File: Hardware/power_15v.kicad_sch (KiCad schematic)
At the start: 13 parts, among them U3 TPS563200, U4 AMS1117-3.3

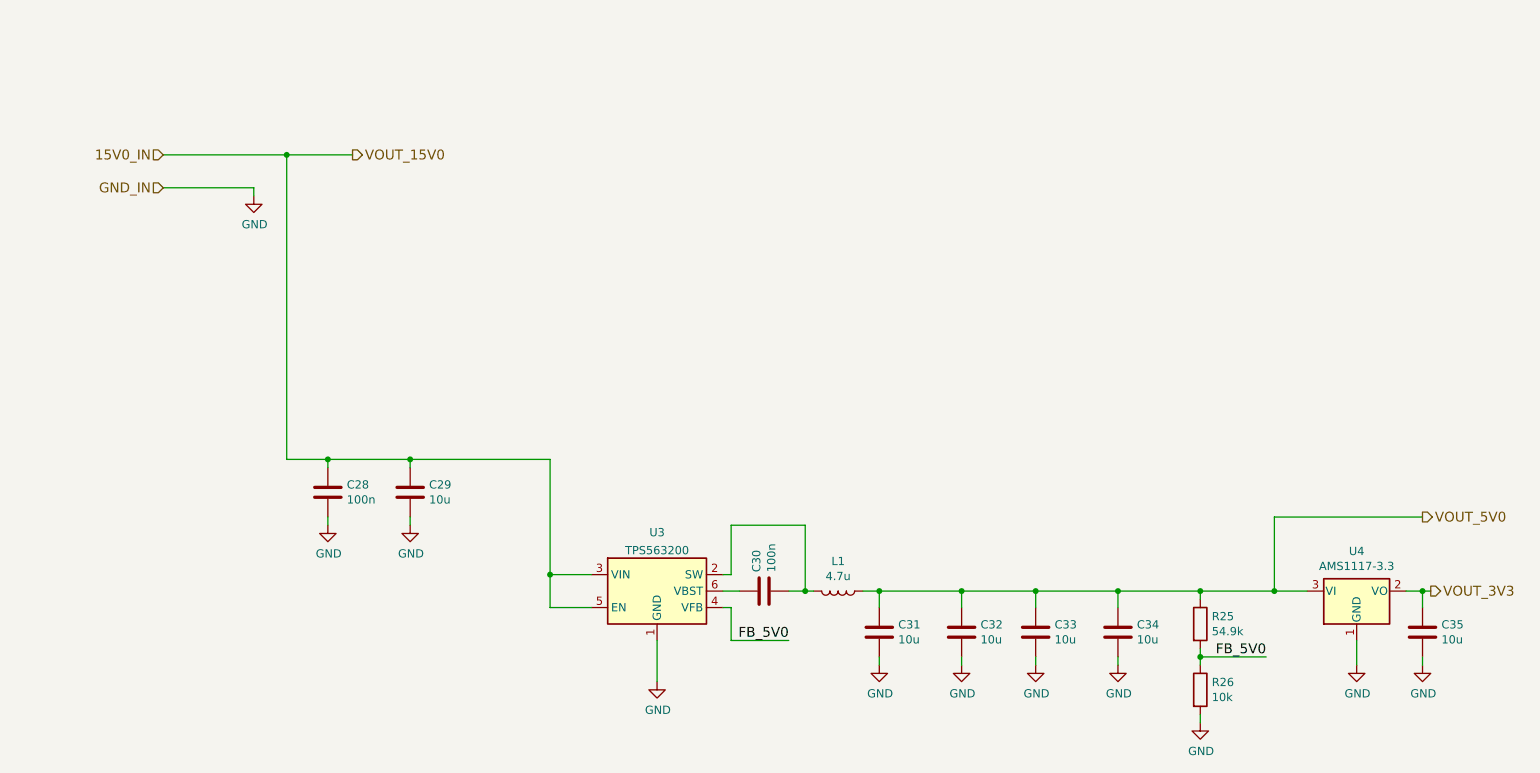
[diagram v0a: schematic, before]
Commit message: feat: updated amplifier IC, finalized design
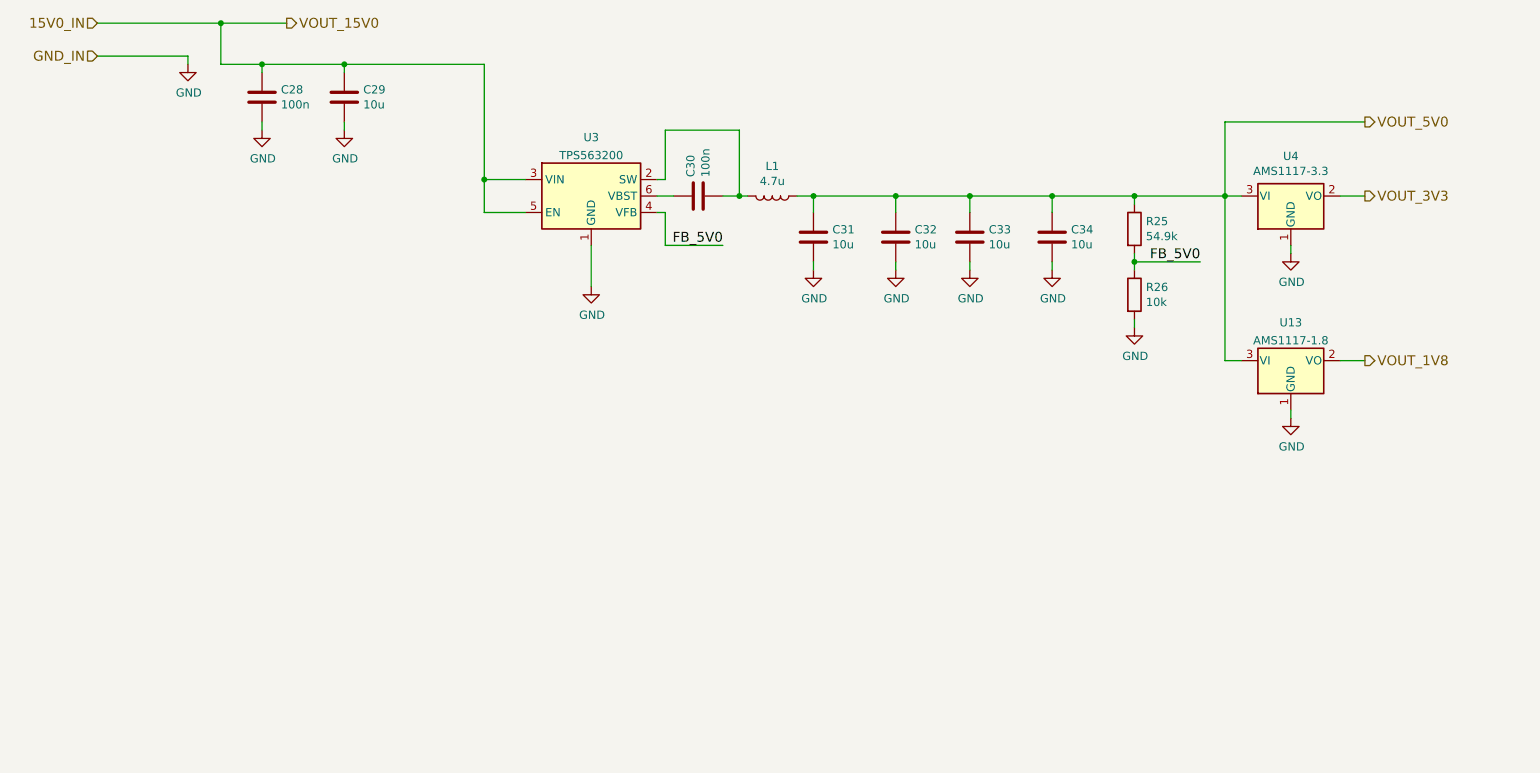
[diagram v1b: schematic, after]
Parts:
- removed C35: 10u, Capacitor_SMD:C_1206_3216Metric_Pad1.33x1.80mm_HandSolder, symbol Device:C
- added U13: AMS1117-1.8, Package_TO_SOT_SMD:SOT-223-3_TabPin2, symbol Regulator_Linear:AMS1117-1.8
- C28, C30: footprint Capacitor_SMD:C_0603_1608Metric_Pad1.08x0.95mm_HandSolder -> Capacitor_SMD:C_0402_1005Metric
- C29, C31, C32, C33, C34: footprint Capacitor_SMD:C_1206_3216Metric_Pad1.33x1.80mm_HandSolder -> Capacitor_SMD:C_1206_3216Metric
- R25, R26: footprint Resistor_SMD:R_0603_1608Metric_Pad0.98x0.95mm_HandSolder -> Resistor_SMD:R_0402_1005Metric
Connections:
- net GND: now also U13.1 (GND)
- net VOUT_5V0: now also U13.3 (VI)
- new net VOUT_1V8: U13.2 (VO)
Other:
- moved on the sheet: C28, C29, C30, C31, C32, C33, C34, L1, R25, R26, U3, U4

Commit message: prod. version blus mini a
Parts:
- removed U3: TPS563200, Package_TO_SOT_SMD:SOT-23-6, symbol Regulator_Switching:TPS563200
- added R10: 4.7k, Resistor_SMD:R_0402_1005Metric, symbol Device:R
- added R11, R12: 10k, Resistor_SMD:R_0402_1005Metric, symbol Device:R
- added U7: TPS54302, Package_TO_SOT_SMD:SOT-23-6, symbol Regulator_Switching:TPS54302
- C53: renamed from C29; MPN (none) -> C13585
- C54: renamed from C28; MPN (none) -> C307331
- C55: renamed from C30; MPN (none) -> C307331
- C56: renamed from C34; MPN (none) -> C13585
- C57: renamed from C33; MPN (none) -> C13585
- C58: renamed from C32; MPN (none) -> C13585
- C59: renamed from C31; MPN (none) -> C13585
- R13: renamed from R26; value 10k -> 13.7k
- R14: renamed from R25; value 54.9k -> 100k; MPN (none) -> C25741
- U5: renamed from U4; JLCPCB Rotation Offset (none) -> 180; MPN (none) -> C6186
- U6: renamed from U13; JLCPCB Rotation Offset (none) -> 180
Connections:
- net FB_5V0: now also U7.4 (FB)
- net GND: now also R10.1, U7.1 (GND)
- net at L1.2: now also C55.1, U7.2 (SW); no longer C55.2
- net 15V0_IN renamed VPP
- net VPP: now also R12.2, U7.3 (VIN)
- new net: C55.2, U7.6 (BOOT)
- new net: R10.2, R11.1, U7.5 (EN)
- new net: R11.2, R12.1
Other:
- note added: "0.6 V * (1 + 100e3 / 13.7e3)"
- note added: "Enable above 1.21 V Divider 0.19 -> 6.37 V min."
- note added: "Pin-compatible: TPS54202 TPS54302 LMR51430"
- moved on the sheet: C55

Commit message: feat!: wip, version b
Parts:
- L1, R13, U6: Mfr.Nr. (none) -> DK
- U7: Mfr.Nr. (none) -> M/DK
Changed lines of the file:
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@@
       (effects (font (size 1.27 1.27)) hide)
     )
-    (property "Mfr.Nr." "" (id 4) (at 140.97 69.85 0)
+    (property "Mfr.Nr." "DK" (id 4) (at 140.97 69.85 0)
       (effects (font (size 1.27 1.27)) hide)
     )
@@
       (effects (font (size 1.27 1.27)) hide)
     )
-    (property "Mfr.Nr." "" (id 4) (at 196.85 85.09 0)
+    (property "Mfr.Nr." "DK" (id 4) (at 196.85 85.09 0)
       (effects (font (size 1.27 1.27)) hide)
     )
@@
       (effects (font (size 1.27 1.27)) hide)
     )
-    (property "Mfr.Nr." "" (id 4) (at 113.03 69.85 0)
+    (property "Mfr.Nr." "M/DK" (id 4) (at 113.03 69.85 0)
       (effects (font (size 1.27 1.27)) hide)
     )
@@
       (effects (font (size 1.27 1.27)) hide)
     )
-    (property "Mfr.Nr." "" (id 4) (at 220.98 95.25 0)
-      (effects (font (size 1.27 1.27)) hide)
-    )
+    (property "Mfr.Nr." "DK" (id 4) (at 220.98 95.25 0)
+      (effects (font (size 1.27 1.27)) hide)
+    )
